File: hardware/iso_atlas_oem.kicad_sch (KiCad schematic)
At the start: 4 parts, among them J4 Conn_Coaxial, J5 Conn_Coaxial, U3 Atlas Scientific OEM

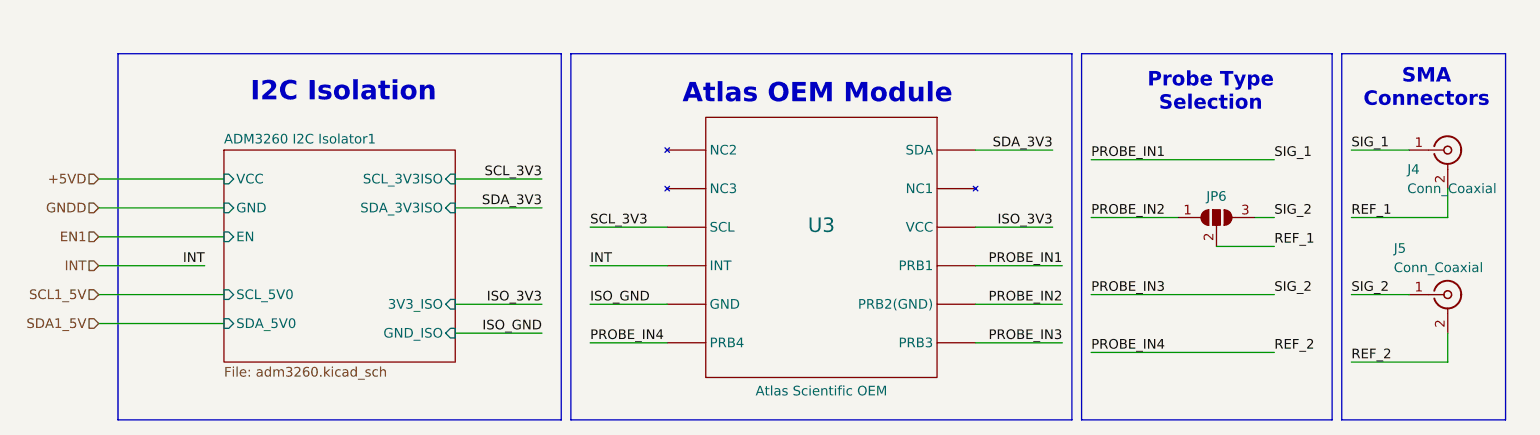
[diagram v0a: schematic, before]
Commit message: removed legacy folders
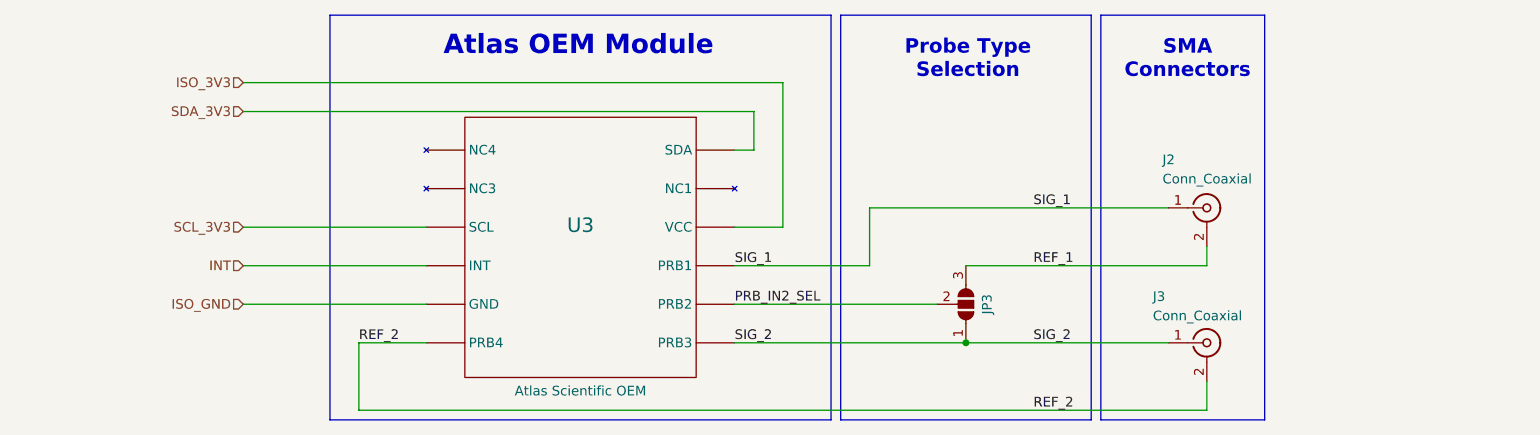
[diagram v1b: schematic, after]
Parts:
- U3: footprint Atlas-Scientific:Atlas_OEM -> kml-custom:Atlas_OEM
- renumbered J4 to J2, J5 to J3, JP6 to JP3
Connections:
- net INT: now also U3.P9 (INT); no longer U3.P7 (INT)
- net ISO_GND: now also U3.P8 (GND); no longer U3.P6 (GND)
- net REF_1: now also JP3.3 (B); no longer JP3.2 (C)
- net SCL_3V3: now also U3.P10 (SCL); no longer U3.P8 (SCL)
- net PROBE_IN1 renamed SIG_1
- net PROBE_IN2 renamed PRB_IN2_SEL
- net PRB_IN2_SEL: now also JP3.2 (C); no longer JP3.1 (A)
- removed net PROBE_IN3: J3.1 (In), JP3.3 (B), U3.P5 (PRB4)
- net PROBE_IN4 renamed REF_2
- net REF_2: now also U3.P7 (PRB4); no longer U3.P5 (PRB4)
- new net SIG_2: J3.1 (In), JP3.1 (A), U3.P6 (PRB3)
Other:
- removed sheet ADM3260 I2C Isolator1
- note removed: "I2C Isolation"
- moved on the sheet: J2, J3, JP3, U3
